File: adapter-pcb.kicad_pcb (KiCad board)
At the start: 4 copper layers, 90.2 x 95.9 mm, 26 parts, among them J1 SS5-80-3.50-X-D-K-XX, J2 DM3BT-DSF-PEJS, U2 LTC4300A-1IMS8_PBF

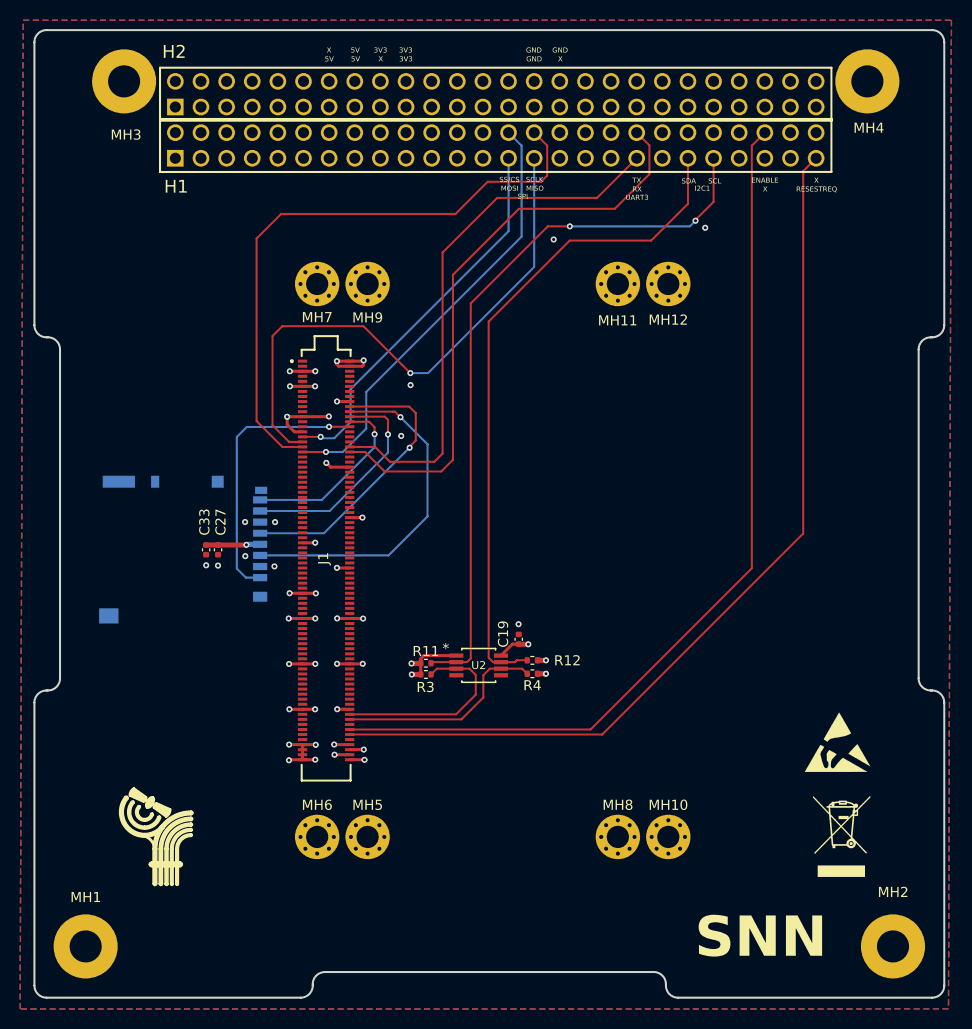
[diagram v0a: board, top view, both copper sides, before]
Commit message: Moved SD Card Slot
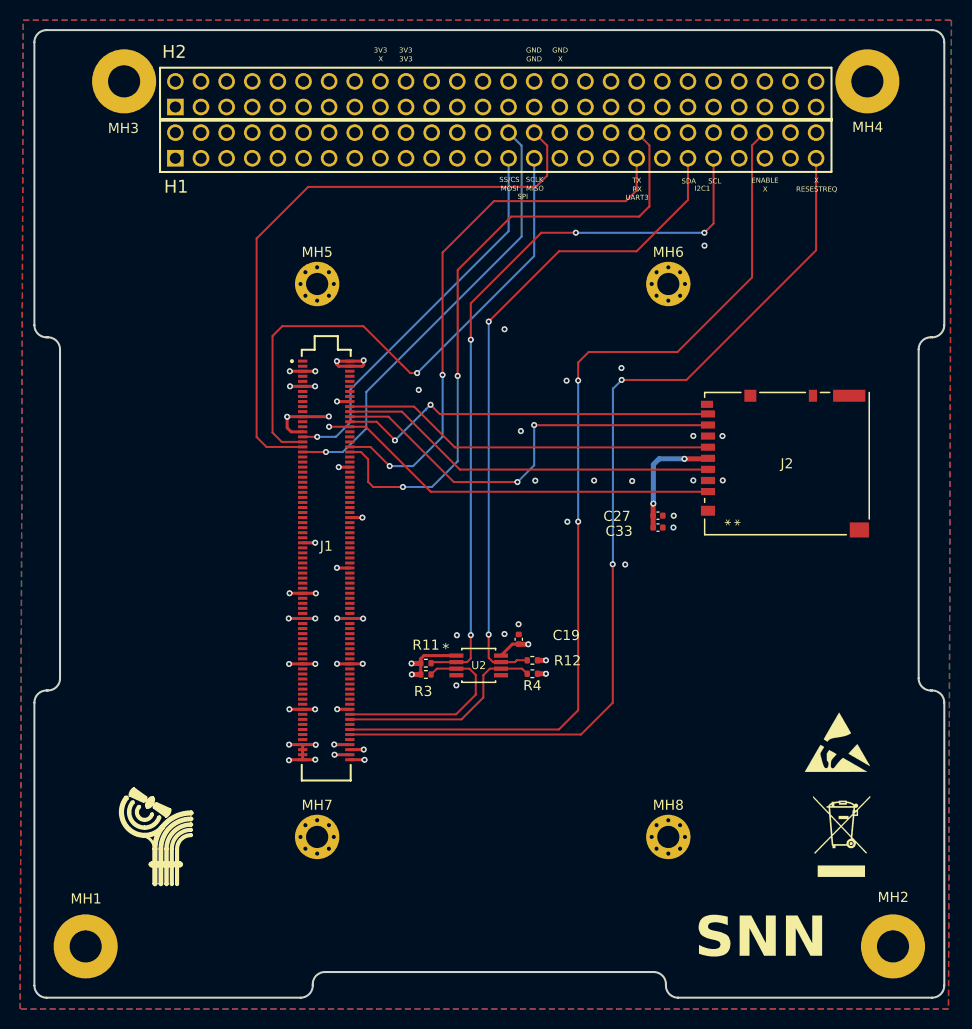
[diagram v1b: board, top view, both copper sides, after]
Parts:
- removed MH10, MH11, MH12, MH9: MountingHole_Pad_MP, MountingHole:MountingHole_2.2mm_M2_Pad_Via
- H1, H2: value Conn_02x26_Odd_Even -> ESQ-126-39-G-D
- J2: moved to F.Cu
- moved MH6 64.9 mm to (168.2, 71.7)
- moved J2 60.6 mm to (180.0, 89.5)
- moved MH5 55.0 mm to (133.4, 71.7)
- moved MH7 54.8 mm to (133.4, 126.5)
- moved C33 44.8 mm to (167.2, 95.8), turned to 0 degrees
- moved C27 43.7 mm to (167.2, 94.6), turned to 0 degrees
- moved MH8 5.00 mm to (168.2, 126.5)
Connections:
- H2 pad 13: +5V -> unconnected-(H2-Pin_13-Pad13)
- H2 pad 15: +5V -> unconnected-(H2-Pin_15-Pad15)
- H2 pad 16: +5V -> unconnected-(H2-Pin_16-Pad16)
- MH5 pad 1: GND -> (no net)
- MH6 pad 1: GND -> (no net)
- MH7 pad 1: GND -> (no net)
- MH8 pad 1: GND -> (no net)
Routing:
- net SD-D0: track 22.2 -> 42.5 mm, vias 1 -> 2
- net SD-D1: track 18.2 -> 37.8 mm, vias 1 -> 2
- net SD-D2: track 27.3 -> 39.8 mm
- net SD-CCLK: track 28.8 -> 36.8 mm, vias 1 -> 0
- net +3V3: track 23.2 -> 29.3 mm, vias 10 -> 11
- net UART_TX: track 58.5 -> 63.3 mm, vias 0 -> 2
- net SNN Enable: track 90.2 -> 93.5 mm, vias 0 -> 2
- net SD-CMD: track 34.4 -> 37.5 mm, vias 1 -> 0
- net RESESTREQ: track 90.9 -> 93.5 mm, vias 0 -> 2
- net UART_RX: track 53.2 -> 54.4 mm, vias 0 -> 2
- net I2C_SCL_CSKB: track 72.1 -> 73.3 mm, vias 2 -> 4
- net GND: track 49.1 -> 47.9 mm, vias 41 -> 51
- net SCLK: track 59.9 -> 60.8 mm
- net I2C_SDA_CSKB: track 66.5 -> 66.3 mm, vias 0 -> 2
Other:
- board text removed: "5V"
